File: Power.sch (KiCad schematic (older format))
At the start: 59 parts, among them J1 Conn_01x02, J2 Conn_01x02, U2 A4403, U3 TPS54531, U4 AP7361C-33E-13

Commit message: started initial layout
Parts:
- F1: value Keystone Fuse Holder -> MOTOR_FUSE
- F2: value Keystone Fuse Holder -> MAIN_POWER_FUSE
- F3: value Keystone Fuse Holder -> BED_FUSE
- F4: value 5A -> BUCK_FUSE_5A
- J1: value Conn_01x02 -> MAIN_POWER
- J2: value Conn_01x02 -> BED_POWER
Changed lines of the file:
@@
 P 1650 1450
 F 0 "J1" H 1568 1125 50  0000 C CNN
-F 1 "Conn_01x02" H 1568 1216 50  0000 C CNN
+F 1 "MAIN_POWER" H 1568 1216 50  0000 C CNN
 F 2 "TerminalBlock_Dinkle:TerminalBlock_Dinkle_DT-55-B01X-02_P10.00mm" H 1650 1450 50  0001 C CNN
 F 3 "~" H 1650 1450 50  0001 C CNN
@@
 P 2100 2300
 F 0 "F1" V 1903 2300 50  0000 C CNN
-F 1 "Keystone Fuse Holder" V 1994 2300 50  0000 C CNN
+F 1 "MOTOR_FUSE" V 1994 2300 50  0000 C CNN
 F 2 "Fuse:Fuseholder_Blade_Mini_Keystone_3568" V 2030 2300 50  0001 C CNN
 F 3 "~" H 2100 2300 50  0001 C CNN
@@
 P 2100 3850
 F 0 "F3" V 1903 3850 50  0000 C CNN
-F 1 "Keystone Fuse Holder" V 1994 3850 50  0000 C CNN
+F 1 "BED_FUSE" V 1994 3850 50  0000 C CNN
 F 2 "Fuse:Fuseholder_Blade_Mini_Keystone_3568" V 2030 3850 50  0001 C CNN
 F 3 "~" H 2100 3850 50  0001 C CNN
@@
 P 2650 1450
 F 0 "J2" H 2568 1125 50  0000 C CNN
-F 1 "Conn_01x02" H 2568 1216 50  0000 C CNN
+F 1 "BED_POWER" H 2568 1216 50  0000 C CNN
 F 2 "TerminalBlock_Dinkle:TerminalBlock_Dinkle_DT-55-B01X-02_P10.00mm" H 2650 1450 50  0001 C CNN
 F 3 "~" H 2650 1450 50  0001 C CNN
@@
 P 2100 3050
 F 0 "F2" V 1903 3050 50  0000 C CNN
-F 1 "Keystone Fuse Holder" V 1994 3050 50  0000 C CNN
+F 1 "MAIN_POWER_FUSE" V 1994 3050 50  0000 C CNN
 F 2 "Fuse:Fuseholder_Blade_Mini_Keystone_3568" V 2030 3050 50  0001 C CNN
 F 3 "~" H 2100 3050 50  0001 C CNN
@@
 P 9700 3900
 F 0 "F4" V 9503 3900 50  0000 C CNN
-F 1 "5A" V 9594 3900 50  0000 C CNN
+F 1 "BUCK_FUSE_5A" V 9594 3900 50  0000 C CNN
 F 2 "Fuse:Fuseholder_Blade_Mini_Keystone_3568" V 9630 3900 50  0001 C CNN
 F 3 "~" H 9700 3900 50  0001 C CNN

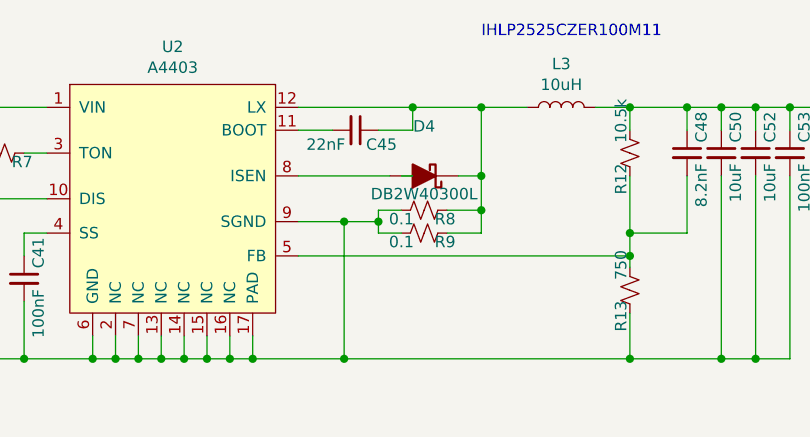
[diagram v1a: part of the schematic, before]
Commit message: Roughtly Layed out power converters and FETs
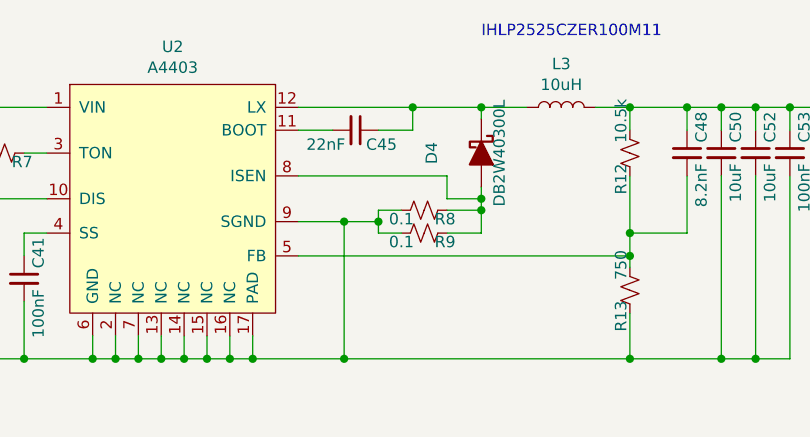
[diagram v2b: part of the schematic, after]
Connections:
- net at C45.1, D4.1 (K), L3.1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: no longer R8.1, R9.1
- net at D4.2 (A), U2.8 (ISEN): now also R8.1, R9.1
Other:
- moved on the sheet: D4
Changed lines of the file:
@@
 L Device:D_Schottky_ALT D4
 U 1 1 5FC97343
-P 7850 1400
-F 0 "D4" H 7850 1183 50  0000 C CNN
-F 1 "DB2W40300L" H 7850 1450 50  0000 C BNN
-F 2 "Diode_SMD:D_SOD-123F" H 7850 1400 50  0001 C CNN
-F 3 "~" H 7850 1400 50  0001 C CNN
-	1    7850 1400
-	-1   0    0    1
-$EndComp
-Wire Wire Line
-	7750 1400 7800 1400
+P 8100 1300
+F 0 "D4" H 8100 1083 50  0000 C CNN
+F 1 "DB2W40300L" H 8100 1350 50  0000 C BNN
+F 2 "Diode_SMD:D_SOD-123F" H 8100 1300 50  0001 C CNN
+F 3 "~" H 8100 1300 50  0001 C CNN
+	1    8100 1300
+	0    1    1    0
+$EndComp
 $Comp
 L Device:R_Small_US R8
@@
 	0    1    1    0
 $EndComp
-Wire Wire Line
-	7800 1100 8100 1100
 Connection ~ 7800 1100
-Wire Wire Line
-	8000 1400 8100 1400
-Wire Wire Line
-	8100 1400 8100 1100
-Connection ~ 8100 1100
-Wire Wire Line
-	8100 1100 8300 1100
-Wire Wire Line
-	7300 1400 7700 1400
 Wire Wire Line
 	7650 1550 7750 1550
@@
 Wire Wire Line
 	8100 1550 8100 1650
-Wire Wire Line
-	8100 1400 8100 1550
-Connection ~ 8100 1400
-Connection ~ 8100 1550
 Wire Wire Line
 	7300 1600 7500 1600
@@
 	1    0    0    -1
 $EndComp
+Wire Wire Line
+	7800 1100 8100 1100
+Wire Wire Line
+	8100 1550 8100 1500
+Connection ~ 8100 1550
+Wire Wire Line
+	8100 1150 8100 1100
+Connection ~ 8100 1100
+Wire Wire Line
+	8100 1100 8300 1100
+Wire Wire Line
+	7950 1400 7950 1500
+Wire Wire Line
+	7950 1500 8100 1500
+Wire Wire Line
+	7300 1400 7950 1400
+Connection ~ 8100 1500
+Wire Wire Line
+	8100 1500 8100 1450
 $EndSCHEMATC
